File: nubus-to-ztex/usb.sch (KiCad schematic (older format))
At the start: 13 parts, among them J6 USB micro-B, U10 SN65220, U11 TPS2051C

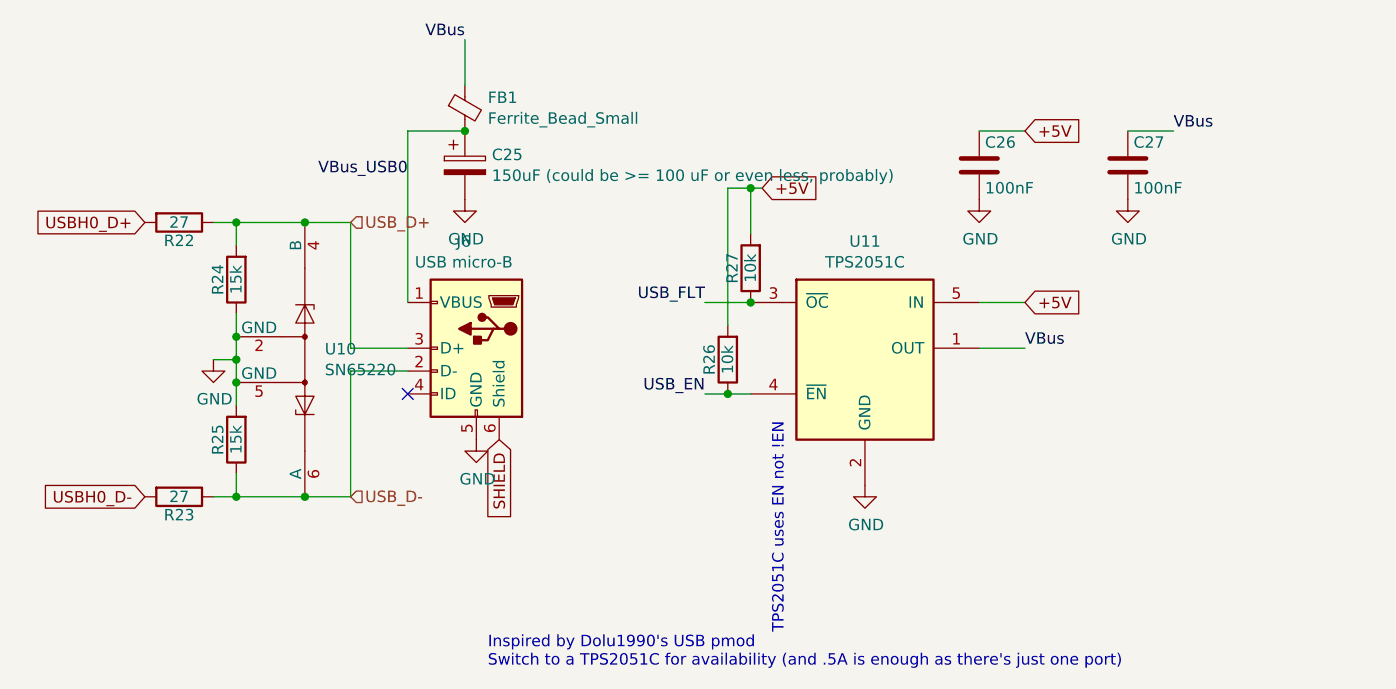
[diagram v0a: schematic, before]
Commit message: more update to V1.2 to try to limit cost
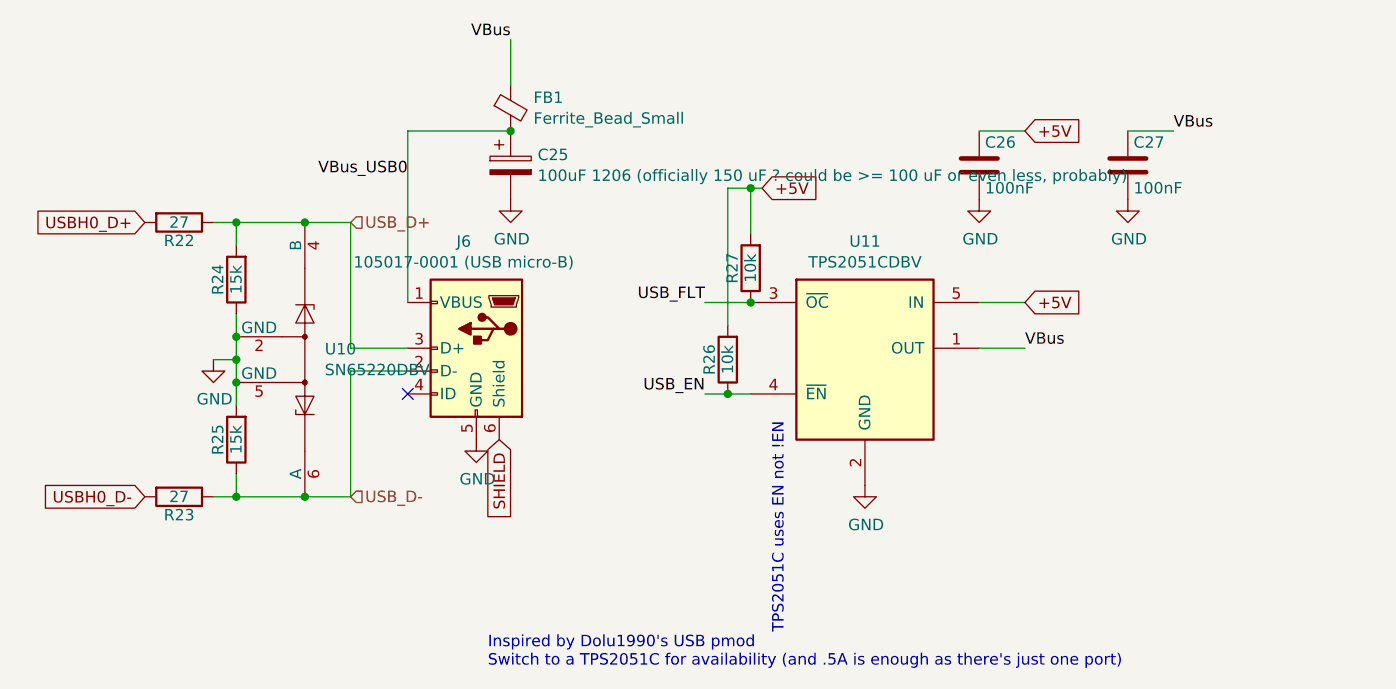
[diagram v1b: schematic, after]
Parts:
- C25: value 150uF (could be >= 100 uF or even less, probably) -> 100uF 1206 (officially 150 uF ? could be >= 100 uF or even less, probably)
- J6: value USB micro-B -> 105017-0001 (USB micro-B)
- U10: value SN65220 -> SN65220DBV
- U11: value TPS2051C -> TPS2051CDBV
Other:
- moved on the sheet: C25, FB1
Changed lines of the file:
@@
 P 5000 2800
 F 0 "J6" H 5055 3267 50  0000 C CNN
-F 1 "USB micro-B" H 5055 3176 50  0000 C CNN
+F 1 "105017-0001 (USB micro-B)" H 5055 3176 50  0000 C CNN
 F 2 "Connector_USB:USB_Micro-B_Molex-105017-0001" H 5150 2750 50  0001 C CNN
 F 3 "https://www.molex.com/pdm_docs/sd/1050170001_sd.pdf" H 5150 2750 50  0001 C CNN
@@
 P 4250 2850
 F 0 "U10" V 4296 2937 50  0000 L CNN
-F 1 "SN65220" V 4205 2937 50  0000 L CNN
+F 1 "SN65220DBV" V 4205 2937 50  0000 L CNN
 F 2 "Package_TO_SOT_SMD:SOT-23-6" H 4600 2700 50  0001 L CNN
 F 3 "http://www.ti.com/lit/ds/symlink/sn65220.pdf" H 4250 3000 50  0001 C CNN
@@
 	3850 2250 3950 2250
 Connection ~ 3950 2250
-Text Label 4950 1450 2    50   ~ 0
+Text Label 5150 1450 2    50   ~ 0
 VBus
 $Comp
@@
 Wire Wire Line
 	4700 1850 4700 2600
-Wire Wire Line
-	4700 1850 4950 1850
 $Comp
 L Device:CP C25
 U 1 1 60D9A750
-P 4950 2000
-F 0 "C25" H 5068 2046 50  0000 L CNN
-F 1 "150uF (could be >= 100 uF or even less, probably)" H 5068 1955 50  0000 L CNN
-F 2 "Capacitor_SMD:C_1206_3216Metric" H 4988 1850 50  0001 C CNN
-F 3 "~" H 4950 2000 50  0001 C CNN
-F 4 "GRM31CR60J157ME11L" H 4950 2000 50  0001 C CNN "MPN-ALT"
-F 5 "https://lcsc.com/product-detail/Multilayer-Ceramic-Capacitors-MLCC-SMD-SMT_Murata-Electronics-GRM31CR60J157ME11L_C528968.html" H 4950 2000 50  0001 C CNN "URL-ALT"
-F 6 "https://www.mouser.fr/ProductDetail/Murata-Electronics/GRM31CR60J157ME11L?qs=qSv5qXjCIG3a12X8fU8miQ%3D%3D" H 4950 2000 50  0001 C CNN "URL-ALT (mouser)"
-F 7 "JMK316ABJ107ML-T" H 4950 2000 50  0001 C CNN "MPN"
-F 8 "https://www.lcsc.com/product-detail/Multilayer-Ceramic-Capacitors-MLCC-SMD-SMT_Taiyo-Yuden-JMK316ABJ107ML-T_C268006.html" H 4950 2000 50  0001 C CNN "URL"
-	1    4950 2000
+P 5150 2000
+F 0 "C25" H 5268 2046 50  0000 L CNN
+F 1 "100uF 1206 (officially 150 uF ? could be >= 100 uF or even less, probably)" H 5268 1955 50  0000 L CNN
+F 2 "Capacitor_SMD:C_1206_3216Metric" H 5188 1850 50  0001 C CNN
+F 3 "~" H 5150 2000 50  0001 C CNN
+F 4 "GRM31CR60J157ME11L" H 5150 2000 50  0001 C CNN "MPN-ALT"
+F 5 "https://lcsc.com/product-detail/Multilayer-Ceramic-Capacitors-MLCC-SMD-SMT_Murata-Electronics-GRM31CR60J157ME11L_C528968.html" H 5150 2000 50  0001 C CNN "URL-ALT"
+F 6 "https://www.mouser.fr/ProductDetail/Murata-Electronics/GRM31CR60J157ME11L?qs=qSv5qXjCIG3a12X8fU8miQ%3D%3D" H 5150 2000 50  0001 C CNN "URL-ALT (mouser)"
+F 7 "JMK316ABJ107ML-T" H 5150 2000 50  0001 C CNN "MPN"
+F 8 "https://www.lcsc.com/product-detail/Multilayer-Ceramic-Capacitors-MLCC-SMD-SMT_Taiyo-Yuden-JMK316ABJ107ML-T_C268006.html" H 5150 2000 50  0001 C CNN "URL"
+	1    5150 2000
 	1    0    0    -1
 $EndComp
@@
 L Device:Ferrite_Bead_Small FB1
 U 1 1 60D9A758
-P 4950 1750
-F 0 "FB1" H 5050 1796 50  0000 L CNN
-F 1 "Ferrite_Bead_Small" H 5050 1705 50  0000 L CNN
-F 2 "Inductor_SMD:L_0805_2012Metric" V 4880 1750 50  0001 C CNN
-F 3 "~" H 4950 1750 50  0001 C CNN
-F 4 "742792022" H 4950 1750 50  0001 C CNN "MPN-ALT"
-F 5 "PZ2012U221-2R0TF" H 4950 1750 50  0001 C CNN "MPN"
-F 6 "https://lcsc.com/product-detail/Ferrite-Beads_Sunlord-PZ2012U221-2R0TF_C44361.html" H 4950 1750 50  0001 C CNN "URL"
-	1    4950 1750
-	1    0    0    -1
-$EndComp
-Connection ~ 4950 1850
-Wire Wire Line
-	4950 1650 4950 1450
+P 5150 1750
+F 0 "FB1" H 5250 1796 50  0000 L CNN
+F 1 "Ferrite_Bead_Small" H 5250 1705 50  0000 L CNN
+F 2 "Inductor_SMD:L_0805_2012Metric" V 5080 1750 50  0001 C CNN
+F 3 "~" H 5150 1750 50  0001 C CNN
+F 4 "742792022" H 5150 1750 50  0001 C CNN "MPN-ALT"
+F 5 "PZ2012U221-2R0TF" H 5150 1750 50  0001 C CNN "MPN"
+F 6 "https://lcsc.com/product-detail/Ferrite-Beads_Sunlord-PZ2012U221-2R0TF_C44361.html" H 5150 1750 50  0001 C CNN "URL"
+	1    5150 1750
+	1    0    0    -1
+$EndComp
+Connection ~ 5150 1850
+Wire Wire Line
+	5150 1650 5150 1450
 $Comp
 L power:GND #PWR0102
 U 1 1 60D9A761
-P 4950 2150
-F 0 "#PWR0102" H 4950 1900 50  0001 C CNN
-F 1 "GND" H 4955 1977 50  0000 C CNN
-F 2 "" H 4950 2150 50  0001 C CNN
-F 3 "" H 4950 2150 50  0001 C CNN
-	1    4950 2150
+P 5150 2150
+F 0 "#PWR0102" H 5150 1900 50  0001 C CNN
+F 1 "GND" H 5155 1977 50  0000 C CNN
+F 2 "" H 5150 2150 50  0001 C CNN
+F 3 "" H 5150 2150 50  0001 C CNN
+	1    5150 2150
 	1    0    0    -1
 $EndComp
@@
 P 6700 2800
 F 0 "U11" H 6700 3267 50  0000 C CNN
-F 1 "TPS2051C" H 6700 3176 50  0000 C CNN
+F 1 "TPS2051CDBV" H 6700 3176 50  0000 C CNN
 F 2 "Package_TO_SOT_SMD:SOT-23-5" H 6700 3300 50  0001 C CNN
 F 3 "" H 6650 3100 50  0001 C CNN
@@
 SHIELD
 NoConn ~ 4700 3000
+Wire Wire Line
+	4700 1850 5150 1850
 $EndSCHEMATC

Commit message: more THT->SMT, lexx expensive parts/assembly (?)
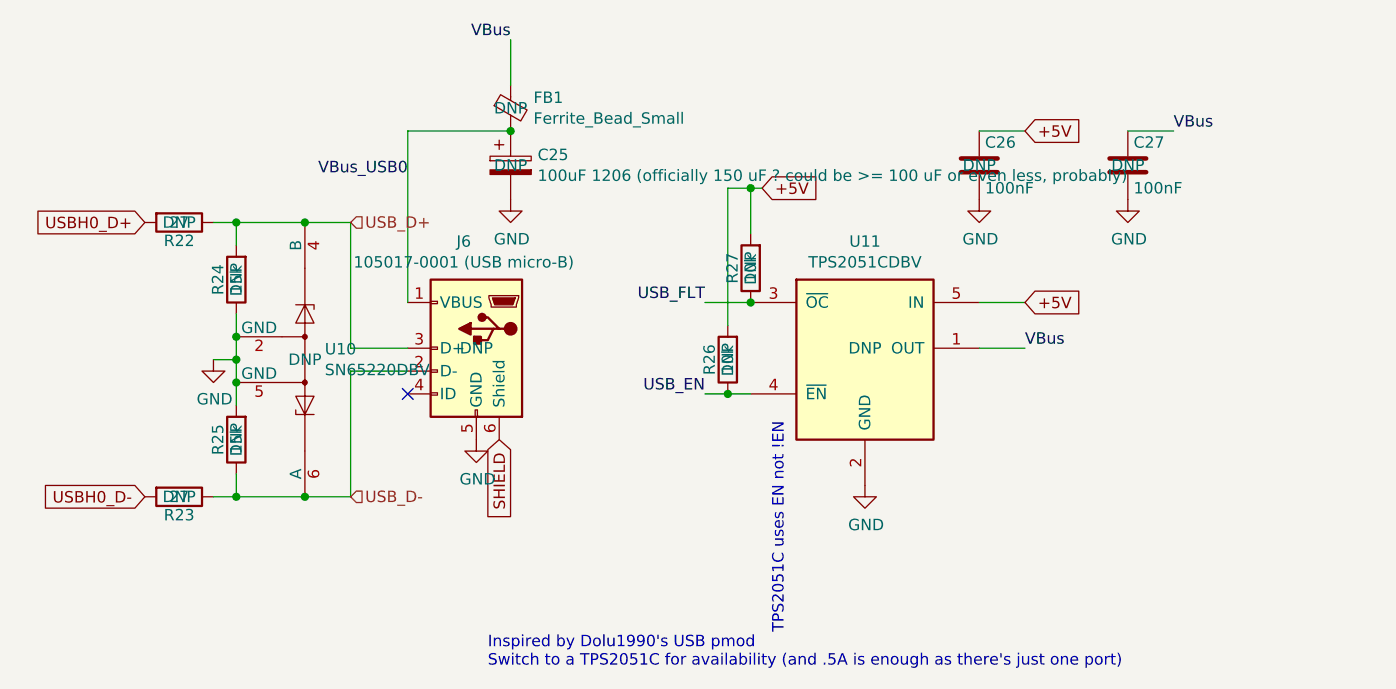
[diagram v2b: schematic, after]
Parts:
- C25, C26, C27, FB1, J6, R22, R23, R24, R25, R26, R27, U10, U11: DNP (none) -> DNP
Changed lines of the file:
@@
 F 6 "https://lcsc.com/product-detail/USB-Connectors_MOLEX-1050170001_C136000.html" H 5000 2800 50  0001 C CNN "URL"
 F 7 "https://www.mouser.fr/ProductDetail/Molex/105017-0001?qs=hlXxxvYE36k7QcsR97GUKA%3D%3D" H 5000 2800 50  0001 C CNN "URL-ALT"
+F 8 "DNP" H 5000 2800 50  0000 C CNN "DNP"
 	1    5000 2800
 	-1   0    0    -1
@@
 F 4 "0603WAF1002T5E" V 6200 1850 50  0001 C CNN "MPN"
 F 5 "https://lcsc.com/product-detail/Chip-Resistor-Surface-Mount_UNI-ROYAL-Uniroyal-Elec-0603WAF1002T5E_C25804.html" V 6200 2450 50  0001 C CNN "URL"
+F 6 "DNP" V 6200 2450 50  0000 C CNN "DNP"
 	1    6200 2450
 	-1   0    0    1
@@
 F 4 "0603WAF1002T5E" V 6100 2250 50  0001 C CNN "MPN"
 F 5 "https://lcsc.com/product-detail/Chip-Resistor-Surface-Mount_UNI-ROYAL-Uniroyal-Elec-0603WAF1002T5E_C25804.html" V 6100 2850 50  0001 C CNN "URL"
+F 6 "DNP" V 6100 2850 50  0000 C CNN "DNP"
 	1    6100 2850
 	-1   0    0    1
@@
 F 10 "TB" H 7200 2000 50  0001 C CNN "Side"
 F 11 "https://lcsc.com/product-detail/Multilayer-Ceramic-Capacitors-MLCC-SMD-SMT_YAGEO-CC0603KRX7R8BB104_C92490.html" H 3000 6050 50  0001 C CNN "URL"
+F 12 "DNP" H 7200 2000 50  0000 C CNN "DNP"
 	1    7200 2000
 	1    0    0    -1
@@
 F 6 "https://www.lcsc.com/product-detail/Others_Texas-Instruments-TI-SN65220DBVT_C350555.html" V 4250 2850 50  0001 C CNN "URL"
 F 7 "SN65220DBVT or SN65220DBVR (Tape or Reel...)" V 4250 2850 50  0001 C CNN "Notes"
+F 8 "DNP" V 4250 2850 50  0000 C CNN "DNP"
 	1    4250 2850
 	0    1    -1   0
@@
 F 4 "0603WAF1502T5E" V 3950 1900 50  0001 C CNN "MPN"
 F 5 "https://lcsc.com/product-detail/Chip-Resistor-Surface-Mount_UNI-ROYAL-Uniroyal-Elec-0603WAF1502T5E_C22809.html" V 3950 2500 50  0001 C CNN "URL"
+F 6 "DNP" V 3950 2500 50  0000 C CNN "DNP"
 	1    3950 2500
 	-1   0    0    1
@@
 F 4 "0603WAF1502T5E" V 3950 2600 50  0001 C CNN "MPN"
 F 5 "https://lcsc.com/product-detail/Chip-Resistor-Surface-Mount_UNI-ROYAL-Uniroyal-Elec-0603WAF1502T5E_C22809.html" V 3950 3200 50  0001 C CNN "URL"
+F 6 "DNP" V 3950 3200 50  0000 C CNN "DNP"
 	1    3950 3200
 	-1   0    0    1
@@
 F 5 "ERJ-3EKF27R0V" V 3700 1650 50  0001 C CNN "MPN-ALT"
 F 6 "https://lcsc.com/product-detail/Chip-Resistor-Surface-Mount_UNI-ROYAL-Uniroyal-Elec-0603WAF270JT5E_C25190.html" V 3700 2250 50  0001 C CNN "URL"
+F 7 "DNP" V 3700 2250 50  0000 C CNN "DNP"
 	1    3700 2250
 	0    1    1    0
@@
 F 5 "ERJ-3EKF27R0V" V 3700 2850 50  0001 C CNN "MPN-ALT"
 F 6 "https://lcsc.com/product-detail/Chip-Resistor-Surface-Mount_UNI-ROYAL-Uniroyal-Elec-0603WAF270JT5E_C25190.html" V 3700 3450 50  0001 C CNN "URL"
+F 7 "DNP" V 3700 3450 50  0000 C CNN "DNP"
 	1    3700 3450
 	0    1    1    0
@@
 F 7 "JMK316ABJ107ML-T" H 5150 2000 50  0001 C CNN "MPN"
 F 8 "https://www.lcsc.com/product-detail/Multilayer-Ceramic-Capacitors-MLCC-SMD-SMT_Taiyo-Yuden-JMK316ABJ107ML-T_C268006.html" H 5150 2000 50  0001 C CNN "URL"
+F 9 "DNP" H 5150 2000 50  0000 C CNN "DNP"
 	1    5150 2000
 	1    0    0    -1
@@
 F 5 "PZ2012U221-2R0TF" H 5150 1750 50  0001 C CNN "MPN"
 F 6 "https://lcsc.com/product-detail/Ferrite-Beads_Sunlord-PZ2012U221-2R0TF_C44361.html" H 5150 1750 50  0001 C CNN "URL"
+F 7 "DNP" H 5150 1750 50  0000 C CNN "DNP"
 	1    5150 1750
 	1    0    0    -1
@@
 F 10 "TB" H 7850 2000 50  0001 C CNN "Side"
 F 11 "https://lcsc.com/product-detail/Multilayer-Ceramic-Capacitors-MLCC-SMD-SMT_YAGEO-CC0603KRX7R8BB104_C92490.html" H 3000 6050 50  0001 C CNN "URL"
+F 12 "DNP" H 7850 2000 50  0000 C CNN "DNP"
 	1    7850 2000
 	1    0    0    -1
@@
 F 6 "https://www.mouser.fr/ProductDetail/Texas-Instruments/TPS2051CDBVR?qs=PF3AD18CSE5vi2HeWLJCmw%3D%3D" H 6700 2800 50  0001 C CNN "URL (Mouser)"
 F 7 "https://lcsc.com/product-detail/Power-Distribution-Switches_Texas-Instruments-TPS2051CDBVR_C129581.html" H 6700 2800 50  0001 C CNN "URL"
+F 8 "DNP" H 6700 2800 50  0000 C CNN "DNP"
 	1    6700 2800
 	1    0    0    -1

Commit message: minor cleanups
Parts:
- C26, C27: LCSC ? -> (none)
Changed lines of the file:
@@
 F 6 "603-CC603KRX7R8BB104" H 7200 2000 50  0001 C CNN "Mouser"
 F 7 "?" H 7200 2000 50  0001 C CNN "Digikey"
-F 8 "?" H 7200 2000 50  0001 C CNN "LCSC"
+F 8 "" H 7200 2000 50  0001 C CNN "LCSC"
 F 9 "?" H 7200 2000 50  0001 C CNN "Koncar"
 F 10 "TB" H 7200 2000 50  0001 C CNN "Side"
@@
 F 6 "603-CC603KRX7R8BB104" H 7850 2000 50  0001 C CNN "Mouser"
 F 7 "?" H 7850 2000 50  0001 C CNN "Digikey"
-F 8 "?" H 7850 2000 50  0001 C CNN "LCSC"
+F 8 "" H 7850 2000 50  0001 C CNN "LCSC"
 F 9 "?" H 7850 2000 50  0001 C CNN "Koncar"
 F 10 "TB" H 7850 2000 50  0001 C CNN "Side"

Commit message: BoM, power plane, serial back to THT, ...
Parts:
- C26, C27: URL https://lcsc.com/product-detail/Multilayer-Ceramic-Capacito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 -> https://www.lcsc.com/product-detail/Multilayer-Ceramic-Capa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
- FB1: URL https://lcsc.com/product-detail/Ferrite-Beads_Sunlord-PZ201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 -> https://www.lcsc.com/product-detail/Ferrite-Beads_Sunlord-P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
- J6: URL https://lcsc.com/product-detail/USB-Connectors_MOLEX-105017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 -> https://www.lcsc.com/product-detail/USB-Connectors_MOLEX-10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
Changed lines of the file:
@@
 F 4 "105017-0001" H 5000 2800 50  0001 C CNN "MPN"
 F 5 "Molex" H 5000 2800 50  0001 C CNN "Manufacturer"
-F 6 "https://lcsc.com/product-detail/USB-Connectors_MOLEX-1050170001_C136000.html" H 5000 2800 50  0001 C CNN "URL"
+F 6 "https://www.lcsc.com/product-detail/USB-Connectors_MOLEX-1050170001_C136000.html" H 5000 2800 50  0001 C CNN "URL"
 F 7 "https://www.mouser.fr/ProductDetail/Molex/105017-0001?qs=hlXxxvYE36k7QcsR97GUKA%3D%3D" H 5000 2800 50  0001 C CNN "URL-ALT"
 F 8 "DNP" H 5000 2800 50  0000 C CNN "DNP"
@@
 F 9 "?" H 7200 2000 50  0001 C CNN "Koncar"
 F 10 "TB" H 7200 2000 50  0001 C CNN "Side"
-F 11 "https://lcsc.com/product-detail/Multilayer-Ceramic-Capacitors-MLCC-SMD-SMT_YAGEO-CC0603KRX7R8BB104_C92490.html" H 3000 6050 50  0001 C CNN "URL"
+F 11 "https://www.lcsc.com/product-detail/Multilayer-Ceramic-Capacitors-MLCC-SMD-SMT_YAGEO-CC0603KRX7R8BB104_C92490.html" H 3000 6050 50  0001 C CNN "URL"
 F 12 "DNP" H 7200 2000 50  0000 C CNN "DNP"
 	1    7200 2000
@@
 F 4 "742792022" H 5150 1750 50  0001 C CNN "MPN-ALT"
 F 5 "PZ2012U221-2R0TF" H 5150 1750 50  0001 C CNN "MPN"
-F 6 "https://lcsc.com/product-detail/Ferrite-Beads_Sunlord-PZ2012U221-2R0TF_C44361.html" H 5150 1750 50  0001 C CNN "URL"
+F 6 "https://www.lcsc.com/product-detail/Ferrite-Beads_Sunlord-PZ2012U221-2R0TF_C44361.html" H 5150 1750 50  0001 C CNN "URL"
 F 7 "DNP" H 5150 1750 50  0000 C CNN "DNP"
 	1    5150 1750
@@
 F 9 "?" H 7850 2000 50  0001 C CNN "Koncar"
 F 10 "TB" H 7850 2000 50  0001 C CNN "Side"
-F 11 "https://lcsc.com/product-detail/Multilayer-Ceramic-Capacitors-MLCC-SMD-SMT_YAGEO-CC0603KRX7R8BB104_C92490.html" H 3000 6050 50  0001 C CNN "URL"
+F 11 "https://www.lcsc.com/product-detail/Multilayer-Ceramic-Capacitors-MLCC-SMD-SMT_YAGEO-CC0603KRX7R8BB104_C92490.html" H 3000 6050 50  0001 C CNN "URL"
 F 12 "DNP" H 7850 2000 50  0000 C CNN "DNP"
 	1    7850 2000

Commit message: some BoM optimization
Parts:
- C25: value 100uF 1206 (officially 150 uF ? could be >= 100 uF or even less, probably) -> 100uF 1206 (officially 150 uF ? could be >= 100 uF or even less probably)
- C26, C27: MPN CC0603KRX7R8BB104 -> CC0603KRX7R9BB104; URL https://www.lcsc.com/product-detail/Multilayer-Ceramic-Capacitors-MLCC-SMD-SMT_YAGEO-CC0603KRX7R8BB104_C92490.html -> https://www.lcsc.com/product-detail/Multilayer-Ceramic-Capacitors-MLCC-SMD-SMT_YAGEO-CC0603KRX7R9BB104_C14663.html
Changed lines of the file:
@@
 F 3 "" H 7200 2000 50  0000 C CNN
 F 4 "www.yageo.com" H 7200 2000 50  0001 C CNN "MNF1_URL"
-F 5 "CC0603KRX7R8BB104" H 7200 2000 50  0001 C CNN "MPN"
+F 5 "CC0603KRX7R9BB104" H 7200 2000 50  0001 C CNN "MPN"
 F 6 "603-CC603KRX7R8BB104" H 7200 2000 50  0001 C CNN "Mouser"
 F 7 "?" H 7200 2000 50  0001 C CNN "Digikey"
@@
 F 9 "?" H 7200 2000 50  0001 C CNN "Koncar"
 F 10 "TB" H 7200 2000 50  0001 C CNN "Side"
-F 11 "https://www.lcsc.com/product-detail/Multilayer-Ceramic-Capacitors-MLCC-SMD-SMT_YAGEO-CC0603KRX7R8BB104_C92490.html" H 3000 6050 50  0001 C CNN "URL"
+F 11 "https://www.lcsc.com/product-detail/Multilayer-Ceramic-Capacitors-MLCC-SMD-SMT_YAGEO-CC0603KRX7R9BB104_C14663.html" H 3000 6050 50  0001 C CNN "URL"
 F 12 "DNP" H 7200 2000 50  0000 C CNN "DNP"
 	1    7200 2000
@@
 P 5150 2000
 F 0 "C25" H 5268 2046 50  0000 L CNN
-F 1 "100uF 1206 (officially 150 uF ? could be >= 100 uF or even less, probably)" H 5268 1955 50  0000 L CNN
+F 1 "100uF 1206 (officially 150 uF ? could be >= 100 uF or even less probably)" H 5268 1955 50  0000 L CNN
 F 2 "Capacitor_SMD:C_1206_3216Metric" H 5188 1850 50  0001 C CNN
 F 3 "~" H 5150 2000 50  0001 C CNN
@@
 F 3 "" H 7850 2000 50  0000 C CNN
 F 4 "www.yageo.com" H 7850 2000 50  0001 C CNN "MNF1_URL"
-F 5 "CC0603KRX7R8BB104" H 7850 2000 50  0001 C CNN "MPN"
+F 5 "CC0603KRX7R9BB104" H 7850 2000 50  0001 C CNN "MPN"
 F 6 "603-CC603KRX7R8BB104" H 7850 2000 50  0001 C CNN "Mouser"
 F 7 "?" H 7850 2000 50  0001 C CNN "Digikey"
@@
 F 9 "?" H 7850 2000 50  0001 C CNN "Koncar"
 F 10 "TB" H 7850 2000 50  0001 C CNN "Side"
-F 11 "https://www.lcsc.com/product-detail/Multilayer-Ceramic-Capacitors-MLCC-SMD-SMT_YAGEO-CC0603KRX7R8BB104_C92490.html" H 3000 6050 50  0001 C CNN "URL"
+F 11 "https://www.lcsc.com/product-detail/Multilayer-Ceramic-Capacitors-MLCC-SMD-SMT_YAGEO-CC0603KRX7R9BB104_C14663.html" H 3000 6050 50  0001 C CNN "URL"
 F 12 "DNP" H 7850 2000 50  0000 C CNN "DNP"
 	1    7850 2000
